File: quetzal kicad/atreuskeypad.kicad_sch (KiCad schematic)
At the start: 209 parts, among them SW1 SW_PUSH, SW10 SW_PUSH, SW100 SW_PUSH, SW101 SW_PUSH, SW102 SW_PUSH, SW103 SW_PUSH, SW104 SW_PUSH, SW11 SW_PUSH, SW12 SW_PUSH, SW13 SW_PUSH, SW14 SW_PUSH, SW15 SW_PUSH, SW16 SW_PUSH, SW17 SW_PUSH, SW18 SW_PUSH, SW19 SW_PUSH, SW2 SW_PUSH, SW20 SW_PUSH, SW21 SW_PUSH, SW22 SW_PUSH, SW23 SW_PUSH, SW24 SW_PUSH, SW25 SW_PUSH, SW26 SW_PUSH, SW27 SW_PUSH, SW28 SW_PUSH, SW29 SW_PUSH, SW3 SW_PUSH, SW30 SW_PUSH, SW31 SW_PUSH, SW32 SW_PUSH, SW33 SW_PUSH, SW34 SW_PUSH, SW35 SW_PUSH, SW36 SW_PUSH, SW37 SW_PUSH, SW38 SW_PUSH, SW39 SW_PUSH, SW4 SW_PUSH, SW40 SW_PUSH, SW41 SW_PUSH, SW42 SW_PUSH, SW43 SW_PUSH, SW44 SW_PUSH, SW45 SW_PUSH, SW46 SW_PUSH, SW47 SW_PUSH, SW48 SW_PUSH, SW49 SW_PUSH, SW5 SW_PUSH, SW50 SW_PUSH, SW51 SW_PUSH, SW52 SW_PUSH, SW53 SW_PUSH, SW54 SW_PUSH, SW55 SW_PUSH, SW56 SW_PUSH, SW57 SW_PUSH, SW58 SW_PUSH, SW59 SW_PUSH, SW6 SW_PUSH, SW60 SW_PUSH, SW61 SW_PUSH, SW62 SW_PUSH, SW63 SW_PUSH, SW64 SW_PUSH, SW65 SW_PUSH, SW66 SW_PUSH, SW67 SW_PUSH, SW68 SW_PUSH, SW69 SW_PUSH, SW7 SW_PUSH, SW70 SW_PUSH, SW71 SW_PUSH, SW72 SW_PUSH, SW73 SW_PUSH, SW74 SW_PUSH, SW75 SW_PUSH, SW76 SW_PUSH, SW77 SW_PUSH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

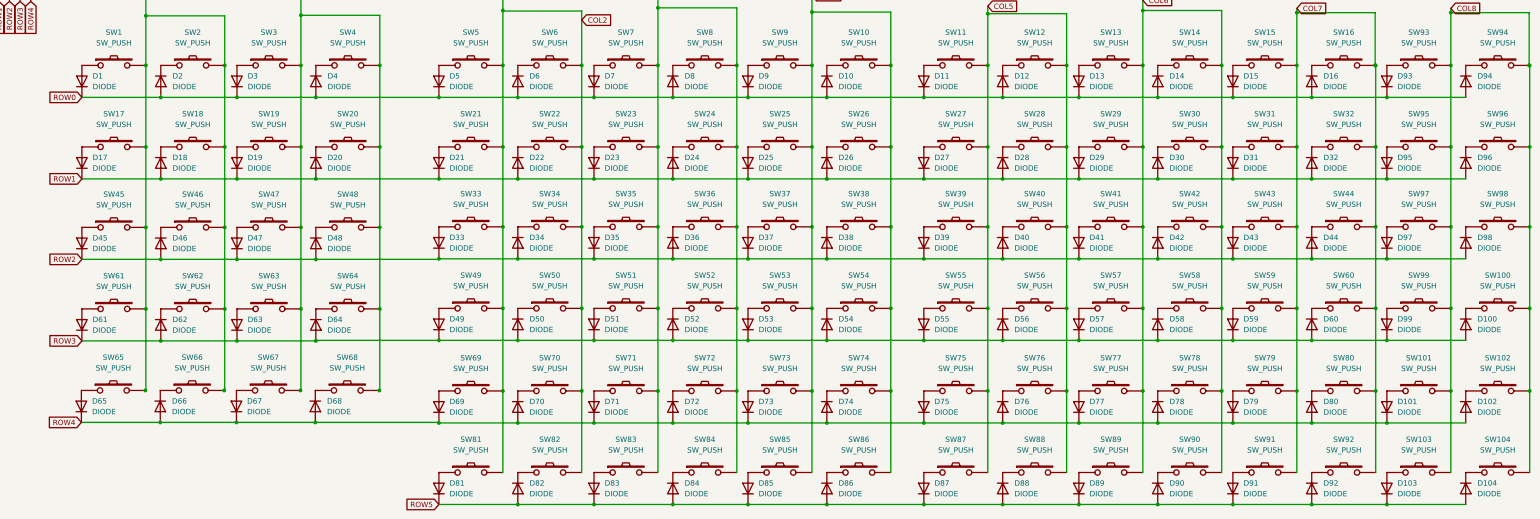
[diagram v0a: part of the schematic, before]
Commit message: fixed backwards diode in schematic
spice_simulation diode symbols are backwards compared to their PCB footprint.  Changed all spice_simulation diode symbols to 1N4148W symbols and verified PCB now matches.
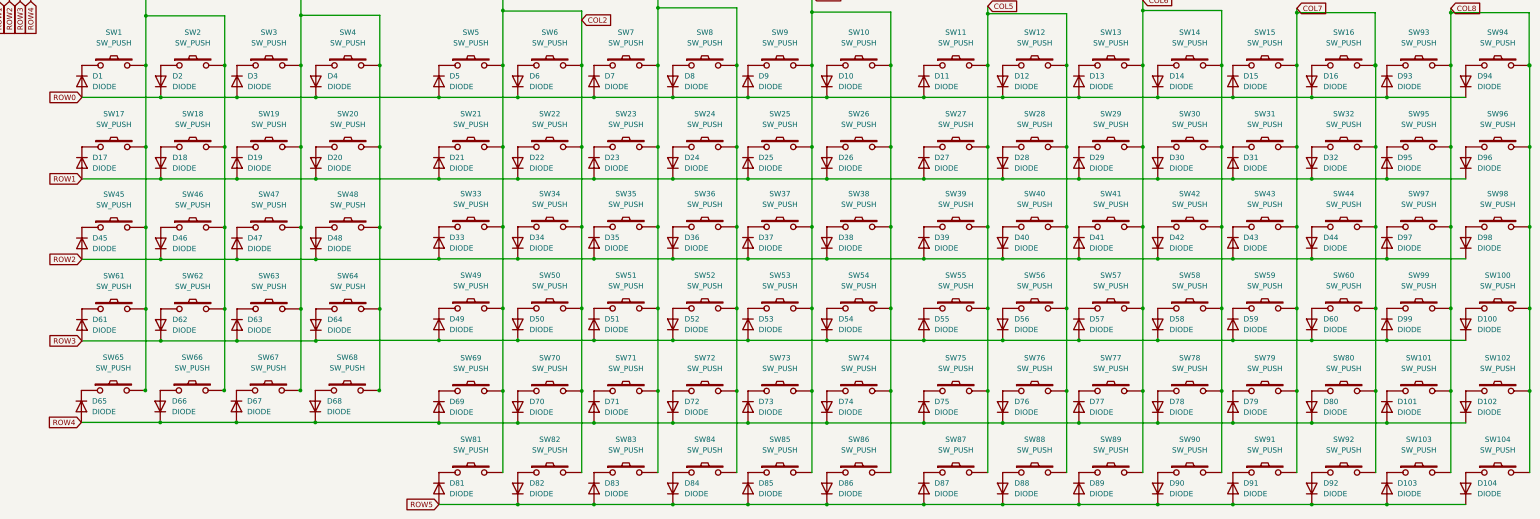
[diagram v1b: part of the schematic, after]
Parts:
- D1, D10, D100, D101, D102, D103, D104, D11, D12, D13, D14, D15, D16, D17, D18, D19, D2, D20, D21, D22, D23, D24, D25, D26, D27, D28, D29, D3, D30, D31, D32, D33, D34, D35, D36, D37, D38, D39, D4, D40, D41, D42, D43, D44, D45, D46, D47, D48, D49, D5, D50, D51, D52, D53, D54, D55, D56, D57, D58, D59, D6, D60, D61, D62, D63, D64, D65, D66, D67, D68, D69, D7, D70, D71, D72, D73, D74, D75, D76, D77, D78, D79, D8, D80, D81, D82, D83, D84, D85, D86, D87, D88, D89, D9, D90, D91, D92, D93, D94, D95, D96, D97, D98, D99: symbol Simulation_SPICE:DIODE -> Diode:1N4148W
- SW1, SW10, SW100, SW101, SW102, SW103, SW104, SW11, SW12, SW13, SW14, SW15, SW16, SW17, SW18, SW19, SW2, SW20, SW21, SW22, SW23, SW24, SW25, SW26, SW27, SW28, SW29, SW3, SW30, SW31, SW32, SW33, SW34, SW35, SW36, SW37, SW38, SW39, SW4, SW40, SW41, SW42, SW43, SW44, SW45, SW46, SW47, SW48, SW49, SW5, SW50, SW51, SW52, SW53, SW54, SW55, SW56, SW57, SW58, SW59, SW6, SW60, SW61, SW62, SW63, SW64, SW65, SW66, SW67, SW68, SW69, SW7, SW70, SW71, SW72, SW73, SW74, SW75, SW76, SW77, SW78, SW79, SW8, SW80, SW81, SW82, SW83, SW84, SW85, SW86, SW87, SW88, SW89, SW9, SW90, SW91, SW92, SW93, SW94, SW95, SW96, SW97, SW98, SW99: footprint (none) -> kbd:CherryMX_1u
